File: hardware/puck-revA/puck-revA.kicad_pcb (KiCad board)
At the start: 2 copper layers, 50 x 50 mm, 32 parts, among them J1 USB-C 16P, J2 UART, J3 EXP (DNP on the product), SW1 BOOT, SW2 RESET, SW3 USER, U1 ESP32-S3-WROOM-1-N16, U2 AP2112K-3.3, U3 74AHCT1G125, U4 USBLC6-2SC6, U5 ambient light, DNP

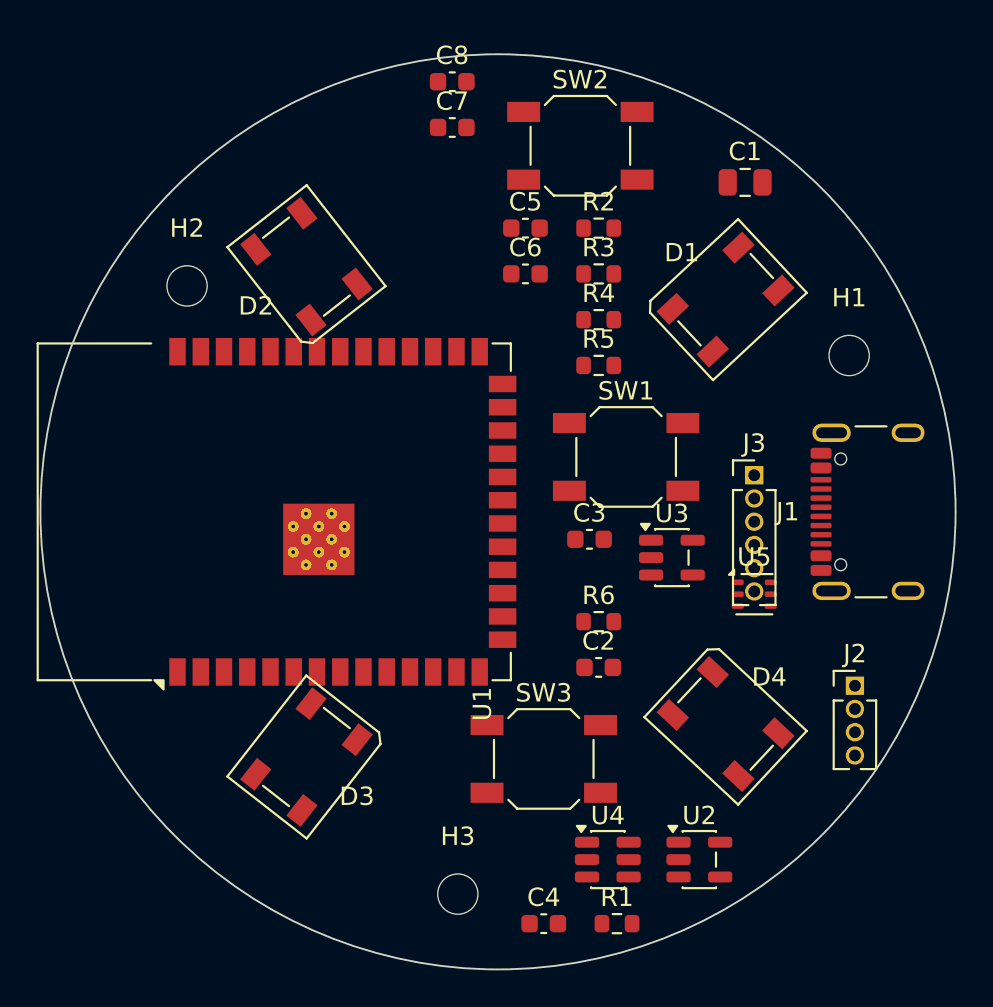
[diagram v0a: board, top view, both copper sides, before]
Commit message: hardware(puck): the antenna moves to the roof, and the light becomes a ring
Two of the LEDs were touching the module. That is a symptom: the -1's trace
antenna has to sit at a board edge and drags a 48 x 41 mm keepout with it, and on
a 50 mm disc that blocked a third of every ring radius permanently. It is what
forced four LEDs instead of three, the asymmetric angles, the 42 mm bolt circle
and the crowding.

So the module is an ESP32-S3-WROOM-1U now: same 41 pins, same 16 MB, a U.FL where
the antenna was. A 2.4 GHz flex adheres inside the diffuser roof and the module
moves to the CENTRE of the board, where its castellated pads face outward at
everything they need to reach. The ring goes round it: eleven SK6812-RGBW on
r=17 at 30 deg, the twelfth slot left empty because that is where the connector
is. Cost is one FPC antenna and a U.FL press at assembly. Modular certification
later depends on using an antenna from Espressif's approved list, which is
written down now rather than discovered later. KiCad ships the -1U footprint but
not its symbol -- the -1's is pin-identical, checked pad for pad -- and no -1U
3D model, so it renders as bare pads.

A ring of light AT THE RIM was built, looked at, and rejected. Twenty-one small
LEDs 3.9 mm inside the wall read as a light ring -- a status band, an Echo Dot --
and bead visibly along the bottom of the band where the wall is only 4.6 mm away.
Every board and doc here describes something else: warm, and still; a small,
plain relay object; not a hard point source you can see the die in. That is an
object that glows evenly from within, which you get with fewer emitters further
from the wall, not more of them closer to it. At r=17 they sit 9.0 mm from the
roof and 8.4 mm from the side, deliberately close to equal, so a body whose
orientation nobody can predict glows the same from every angle.

Decoupling went from one cap per LED to four, and that is a decision rather than
a saving: there is nowhere on a single-sided 50 mm board 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
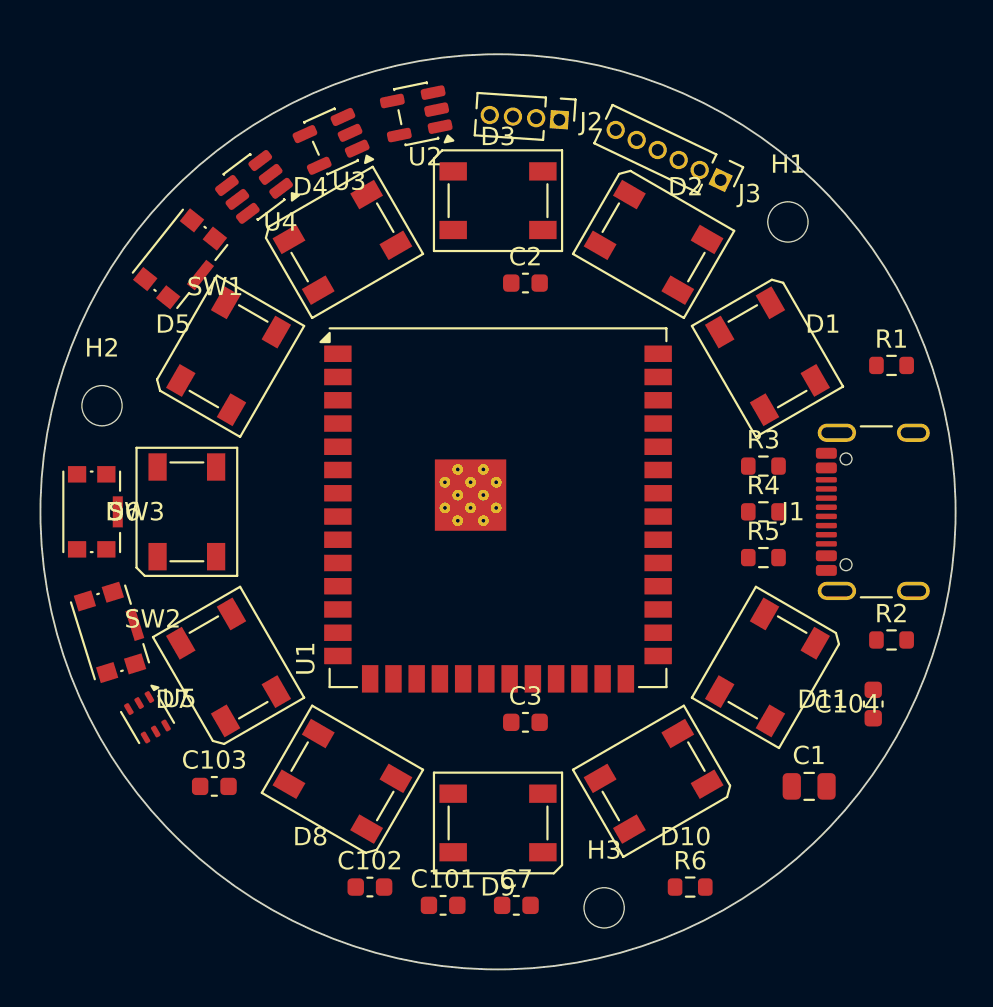
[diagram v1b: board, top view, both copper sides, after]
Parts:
- removed C4, C5, C6, C8: 100n, Capacitor_SMD:C_0603_1608Metric
- added C101: 100n, Capacitor_SMD:C_0603_1608Metric, F.Cu at (97.0, 121.5)
- added C102: 100n, Capacitor_SMD:C_0603_1608Metric, F.Cu at (93.0, 120.5)
- added C103: 100n, Capacitor_SMD:C_0603_1608Metric, F.Cu at (84.5, 115.0)
- added C104: 100n, Capacitor_SMD:C_0603_1608Metric, F.Cu at (120.5, 110.5)
- added D10: SK6812-RGBW, LED_SMD:LED_SK6812_PLCC4_5.0x5.0mm_P3.2mm, F.Cu at (108.5, 114.7)
- added D11: SK6812-RGBW, LED_SMD:LED_SK6812_PLCC4_5.0x5.0mm_P3.2mm, F.Cu at (114.7, 108.5)
- added D5: SK6812-RGBW, LED_SMD:LED_SK6812_PLCC4_5.0x5.0mm_P3.2mm, F.Cu at (85.3, 91.5)
- added D6: SK6812-RGBW, LED_SMD:LED_SK6812_PLCC4_5.0x5.0mm_P3.2mm, F.Cu at (83.0, 100.0)
- added D7: SK6812-RGBW, LED_SMD:LED_SK6812_PLCC4_5.0x5.0mm_P3.2mm, F.Cu at (85.3, 108.5)
- added D8: SK6812-RGBW, LED_SMD:LED_SK6812_PLCC4_5.0x5.0mm_P3.2mm, F.Cu at (91.5, 114.7)
- added D9: SK6812-RGBW, LED_SMD:LED_SK6812_PLCC4_5.0x5.0mm_P3.2mm, F.Cu at (100.0, 117.0)
- SW1, SW2, SW3: footprint Button_Switch_SMD:SW_SPST_SKQG_WithoutStem -> Button_Switch_SMD:SW_Push_1P1T-SH_NO_CK_KMR2xxG
- U1: value ESP32-S3-WROOM-1-N16 -> ESP32-S3-WROOM-1U-N16; footprint RF_Module:ESP32-S3-WROOM-1 -> RF_Module:ESP32-S3-WROOM-1U
- moved U2 43.6 mm to (95.5, 78.3), turned to 191.613 degrees
- moved C7 42.6 mm to (101.0, 121.5)
- moved U4 41.5 mm to (86.7, 82.2), turned to 216.906 degrees
- moved SW2 37.0 mm to (78.8, 106.6), turned to 287.259 degrees
- moved J2 34.9 mm to (103.4, 78.6), turned to 266.152 degrees
- moved R1 34.0 mm to (121.5, 92.0)
- moved U5 33.8 mm to (80.8, 111.2), turned to 300.37 degrees
- moved D4 33.6 mm to (91.5, 85.3), turned to 30 degrees
- moved C1 33.2 mm to (117.0, 115.0)
- moved D3 32.1 mm to (100.0, 83.0), turned to 0 degrees
- moved U3 29.4 mm to (90.9, 79.8), turned to 204.26 degrees
- moved SW3 28.1 mm to (77.8, 100.0), turned to 270 degrees
- moved R2 27.6 mm to (121.5, 107.0)
- moved SW1 26.7 mm to (82.6, 86.2), turned to 231.488 degrees
- moved C2 21.4 mm to (101.5, 87.5)
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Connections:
- D4 pad 2: (no net) -> LED_D4_OUT

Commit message: hardware(puck): label the controls, and stop the silkscreen shouting part numbers
The switches did have labels -- BOOT, RESET, USER as footprint Values -- and you
could not read a single one of them. Auto-placed Value text on a 50 mm disc put
"SK6812-RGBW" on the board eleven times, plus AP2112K-3.3, 74AHCT1G125,
USBLC6-2SC6 and a part number long enough to run off the edge, all on top of each
other and on top of the labels that mattered.

So: every Value is hidden (they live in the BOM and the schematic), and the
things a person hunts for by eye get a deliberate label on the free annulus
between the module and the LED ring -- the one place on this board with room for
text. BOOT, RST, USR on the three switches, UART and EXP on the two headers, each
on the same radial line as the part it names, 1.2 mm and turned to read along the
annulus rather than upside down on the left-hand side.

Reference designators for the LEDs and passives move to F.Fab, which is where
assembly documentation expects them. D1..D11 and C101..C104 auto-placed around a
34 mm ring collide with each other and with everything else, and none of them is
something you read off a silkscreen. The switches, headers, connector, ICs and
mounting holes keep theirs.

SW2 moved from 197 to 210 degrees. At 17 degrees from SW3 the words RST and USR
ran into each other, which is the same failure as the part numbers in miniature.

Silk overlaps: 51 -> 20. The rest are reference designators brushing footprint
outlines, which is ordinary and legible.

Two bugs of my own on the way, both silent. hide_property called top_properties
at the wrong nesting depth -- a footprint's spliced-out contents put properties
at depth 0, not 1 -- so it found nothing and hid nothing without complaining;
top_properties takes the level explicitly now. And top_properties itself lived
only in gen_sch.py, so the first run of this died outright, which was the honest
failure of the two.

Co-Authored-By: Claude Opus 5 (1M context) <noreply@a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
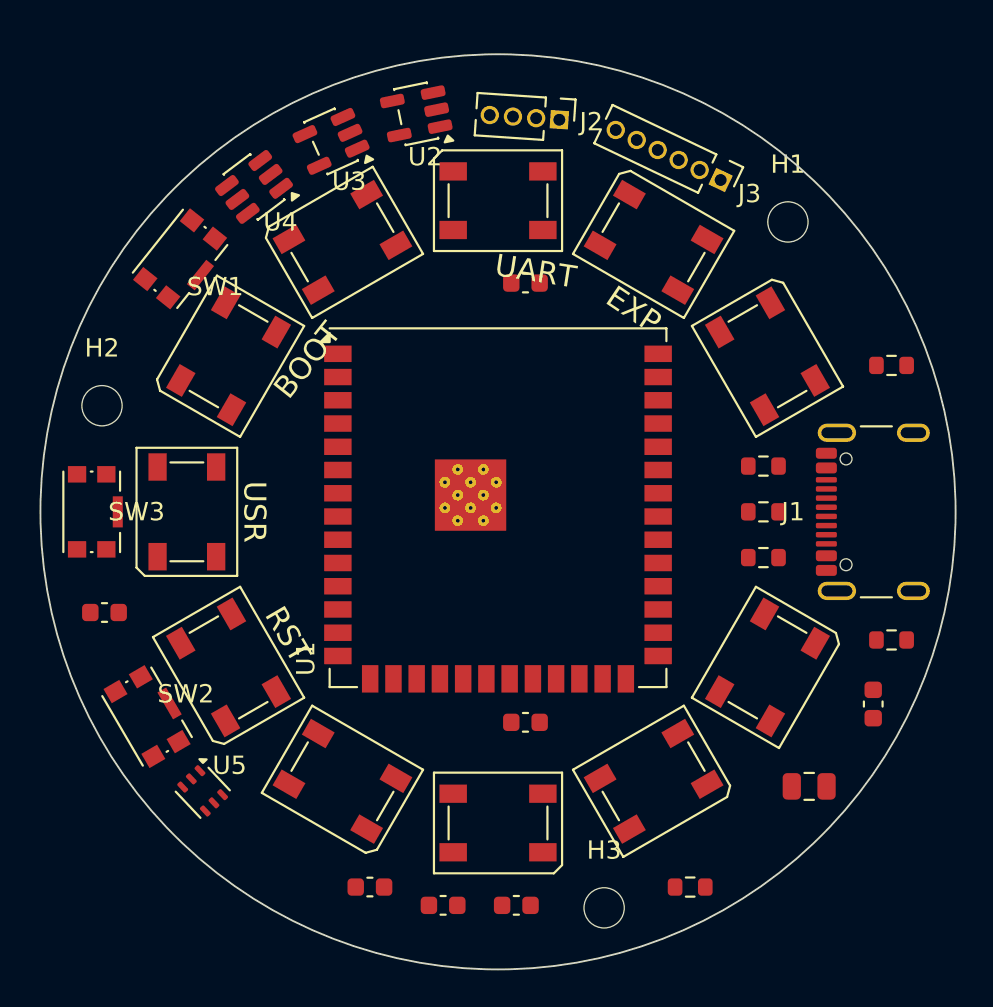
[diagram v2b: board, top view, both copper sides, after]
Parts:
- moved C103 11.2 mm to (78.5, 105.5)
- moved U5 5.03 mm to (83.9, 115.2), turned to 313.37 degrees
- moved SW2 5.03 mm to (80.8, 111.2), turned to 300.259 degrees
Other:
- board text added: "BOOT"
- board text added: "EXP"
- board text added: "RST"
- board text added: "UART"
- board text added: "USR"

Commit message: hardware(puck): place by circuit, not by list order
Checking placement before routing found a diode that protects nothing: U4, the
USB ESD clamp, sat 39 mm from the connector it clamps, because the packer walked
the parts in the order I happened to write them. The 22 uF input bulk was 43 mm
from the regulator it feeds. No amount of routing repairs either.

So the outer ring is assigned by circuit now. R1 and R2 flank J1; C1 sits on U2's
VIN; U3's 5 V output starts beside the chain's first LED. And U4 is pinned rather
than preferred, at r=14.2 directly inboard of the connector -- there is no LED at
0 degrees, that slot is where the connector is -- which puts it 7.1 mm from J1
with D+/D- running straight out to the pads. The outer ring pushed it past the
mounting hole at 45 twice; a preference was not strong enough for something that
only works at the port.

Preferred angles say what belongs near what; a solver makes them fit, spreading
each part by its real courtyard width around the mounting holes and the
connector. Hand-picked angles alone gave seven shorts and ten mask bridges. The
gap between neighbours is 0.7 mm: at 0.45 a header clipped a switch, and at 1.0
the ring overflows and the assert says so by name.

Inboard is not an annulus and the placer now knows it. The module's courtyard
reaches 10.1 mm off its flat faces but 14.0 at its corners, against a LED ring
starting at 14.25 -- so there is room near 0/90/180/270 and none diagonally. Each
small part walks outward from its preferred angle to the first slot that clears.
Checking only the short side of a tangential part let four resistors clip the
module, so the check is conservative: the long half-width both ways.

DRC: no shorts, no clearance violations, no courtyard overlaps, no mask bridges.
What remains is 113 unconnected items -- the netlist waiting to be routed -- silk
that tidies during layout, and the 0.2 mm thermal vias in Espressif's footprint
that JLC's 0.3 mm floor still wants enlarged. Schematic 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
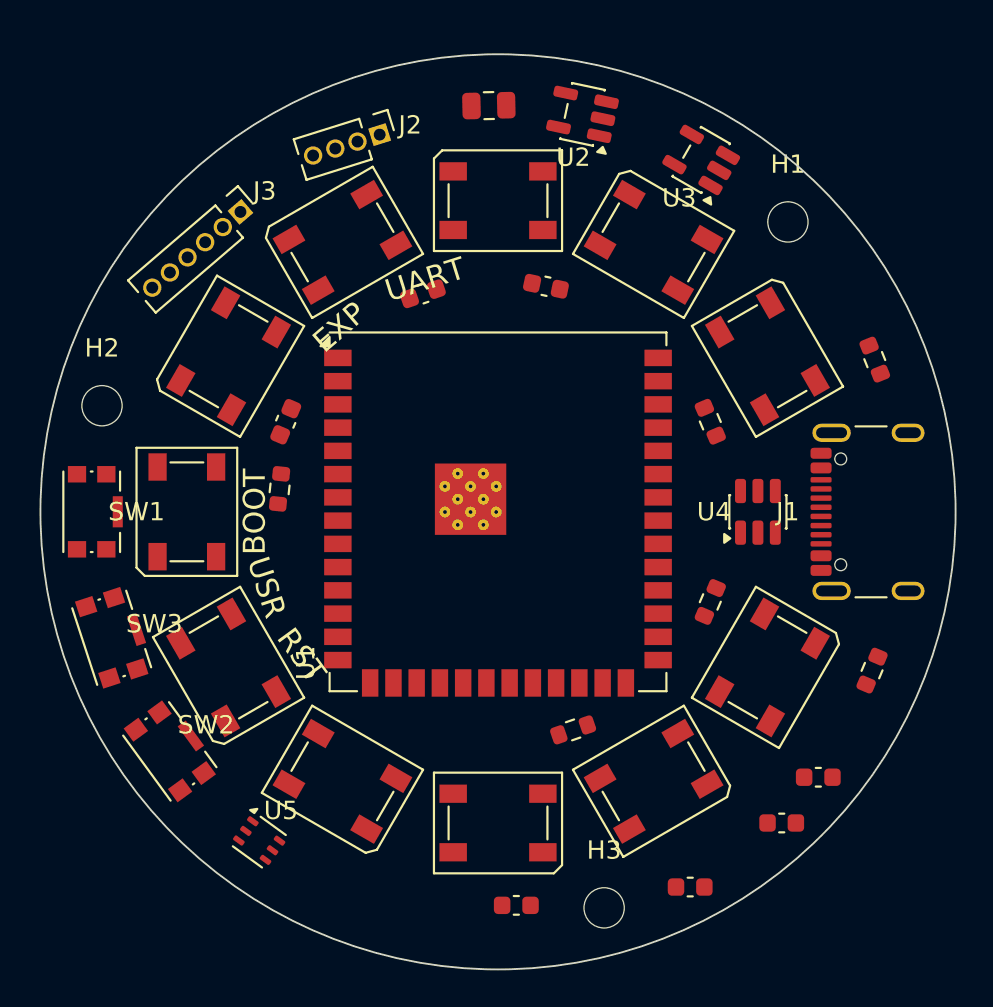
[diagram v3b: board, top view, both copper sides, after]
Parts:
- moved C1 41.1 mm to (99.5, 77.8), turned to 181.292 degrees
- moved C103 35.3 mm to (110.5, 120.5)
- moved C7 33.8 mm to (95.9, 88.1), turned to 199 degrees
- moved U4 32.8 mm to (114.2, 100.0), turned to 90 degrees
- moved R3 26.5 mm to (88.1, 98.7), turned to 264 degrees
- moved J3 26.3 mm to (85.9, 83.6), turned to 310.656 degrees
- moved C102 22.8 mm to (115.5, 117.0)
- moved C104 22.4 mm to (101.0, 121.5), turned to 0 degrees
- moved C101 21.7 mm to (117.5, 114.5)
- moved C3 21.0 mm to (88.4, 95.1), turned to 247 degrees
- moved U3 20.2 mm to (111.1, 80.8), turned to 150 degrees
- moved R6 15.6 mm to (111.6, 104.9), turned to 67 degrees
- moved SW1 14.6 mm to (77.8, 100.0), turned to 269.992 degrees
- moved R5 14.0 mm to (104.1, 111.9), turned to 19 degrees
- moved J2 9.85 mm to (93.5, 79.4), turned to 287.42 degrees
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
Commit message: hardware(puck): pour the ground, chain the ring, and stop short of the rest
route.py adds copper to the board gen_pcb.py places. Separate on purpose: gen_pcb
owns placement and refuses to overwrite copper, so the two cannot fight.

What is routed, and verified by route.py --check:

  GND  -- 57 pads, ONE island. A pour on BOTH layers, which is the whole trick
          and took me far too long to reach. A pour on the component side
          connects every surface-mount ground pad directly, with no via and no
          stub, and KiCad clears it around foreign nets by itself. I first tried
          to stitch ~40 ground pads with hand-rolled geometry and it cost shorts,
          mask bridges and crossing tracks in every arrangement -- writing a bad
          autorouter to solve a problem a pour does not have.
  Chain -- all ten DOUT->DIN hops. Three segments each, not two: a straight
          dogleg cuts across the intervening VSS pad, twenty DRC hits on one pad
          of D9 alone. Down to r=13.6, round, and back out.
  VBUS -- the eleven LED VDD pads, onto a ring on the back at r=18.76 where the
          ring's own geometry puts them. Vias offset ALONG the ring, not across
          it: it is 2.6 mm wide and any radial offset big enough to clear a pad
          leaves it.

Thirteen VBUS pads are named in the output and left alone -- C1 and the LED caps
sit at r~22, outside the ring, and U4 inside it at 14.2. A radial run to reach
them crosses the LED pads (thirteen shorts, twenty-six mask bridges), so that is
the boundary between what symmetry routes and what judgement routes. The signal
nets were never mine to do.

I had the rails backwards at first and put the power pour over the ground pads.
Measuring the placed board rather than reasoning about it is what caught it:
turned tangentially, every LED puts VDD and DIN on the OUTER flank at r=18.76 and
VSS and DOUT on the inner at 15.59.

THE VERIFICATION LIMIT, which matters for reading the DRC report. `kicad-c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
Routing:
- net VBUS: track 0.00 -> 22.0 mm, vias 0 -> 11
- net LED_D8_OUT: track 0.00 -> 10.3 mm
- net LED_D5_OUT: track 0.00 -> 10.3 mm
- net LED_D2_OUT: track 0.00 -> 10.3 mm
- net LED_D9_OUT: track 0.00 -> 10.3 mm
- net LED_D6_OUT: track 0.00 -> 10.3 mm
- net LED_D3_OUT: track 0.00 -> 10.3 mm
- net LED_D7_OUT: track 0.00 -> 10.3 mm
- net LED_D4_OUT: track 0.00 -> 10.3 mm
- net LED_D1_OUT: track 0.00 -> 10.3 mm
- net LED_D10_OUT: track 0.00 -> 10.3 mm
- added copper zone on B.Cu, net GND
- added copper zone on F.Cu, net GND
- added copper zone on B.Cu, net VBUS
